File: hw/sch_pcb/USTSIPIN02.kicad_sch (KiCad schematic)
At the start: 5 parts, among them M1 HOLE, M2 HOLE, M3 HOLE, M4 HOLE, M8 BMI-S-204-F

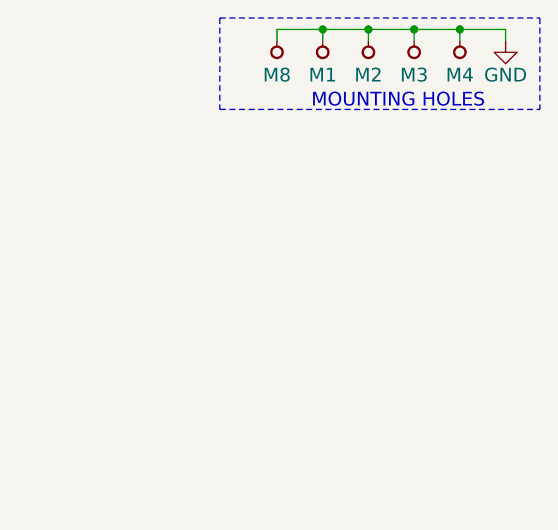
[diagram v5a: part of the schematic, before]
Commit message: Angled USB IC.
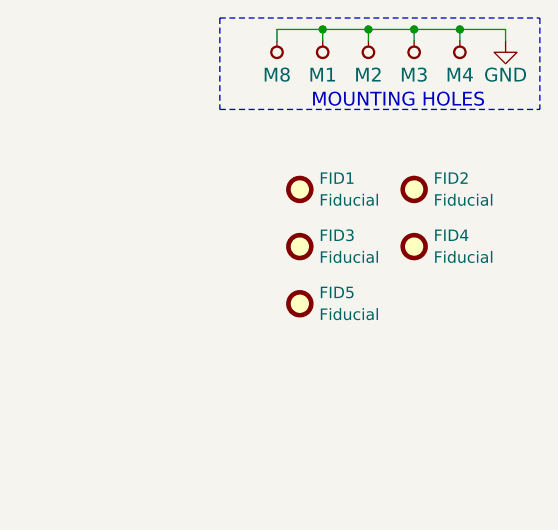
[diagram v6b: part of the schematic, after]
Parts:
- added FID1, FID2, FID3, FID4, FID5: Fiducial, Fiducial:Fiducial_1mm_Mask2mm, symbol Mechanical:Fiducial
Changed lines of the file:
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@@
+    )
+  )
+  (symbol (lib_id "Mechanical:Fiducial") (at 255.27 40.64 0) (unit 1)
+    (in_bom yes) (on_board yes) (dnp no) (fields_autoplaced)
+    (property "Reference" "FID3" (at 257.429 39.4279 0)
+      (effects (font (size 1.27 1.27)) (justify left))
+    )
+    (property "Value" "Fiducial" (at 257.429 41.8521 0)
+      (effects (font (size 1.27 1.27)) (justify left))
+    )
+    (property "Footprint" "Fiducial:Fiducial_1mm_Mask2mm" (at 255.27 40.64 0)
+      (effects (font (size 1.27 1.27)) hide)
+    )
+    (property "Datasheet" "~" (at 255.27 40.64 0)
+      (effects (font (size 1.27 1.27)) hide)
+    )
+    (instances
+      (project "USTSIPIN02"
+        (path "/0a87ced0-2af2-43c5-a56c-218f7013d76f"
+          (reference "FID3") (unit 1)
+        )
+      )
+      (project "PIND02"
+        (path "/2ae32537-a16f-4c5b-a56b-c6dddfb8ddb4"
+          (reference "FID1") (unit 1)
+        )
+      )
+      (project "AIRDOS04_base"
+        (path "/e63e39d7-6ac0-4ffd-8aa3-1841a4541b55/e191f86f-5b54-4b8b-aca6-37b81226f3b6"
+          (reference "FID3") (unit 1)
+        )
+        (path "/e63e39d7-6ac0-4ffd-8aa3-1841a4541b55"
+          (reference "FID3") (unit 1)
+        )
+      )
+    )
+  )
+  (symbol (lib_id "Mechanical:Fiducial") (at 255.27 34.29 0) (unit 1)
+    (in_bom yes) (on_board yes) (dnp no) (fields_autoplaced)
+    (property "Reference" "FID1" (at 257.429 33.0779 0)
+      (effects (font (size 1.27 1.27)) (justify left))
+    )
+    (property "Value" "Fiducial" (at 257.429 35.5021 0)
+      (effects (font (size 1.27 1.27)) (justify left))
+    )
+    (property "Footprint" "Fiducial:Fiducial_1mm_Mask2mm" (at 255.27 34.29 0)
+      (effects (font (size 1.27 1.27)) hide)
+    )
+    (property "Datasheet" "~" (at 255.27 34.29 0)
+      (effects (font (size 1.27 1.27)) hide)
+    )
+    (instances
+      (project "USTSIPIN02"
+        (path "/0a87ced0-2af2-43c5-a56c-218f7013d76f"
+          (reference "FID1") (unit 1)
+        )
+      )
+      (project "AIRDOS04_base"
+        (path "/e63e39d7-6ac0-4ffd-8aa3-1841a4541b55"
+          (reference "FID1") (unit 1)
+        )
+        (path "/e63e39d7-6ac0-4ffd-8aa3-1841a4541b55/5c006114-f78d-4936-a365-c4e7307459e1"
+          (reference "FID1") (unit 1)
+        )
+      )
+    )
+  )
+  (symbol (lib_id "Mechanical:Fiducial") (at 267.97 34.29 0) (unit 1)
+    (in_bom yes) (on_board yes) (dnp no) (fields_autoplaced)
+    (property "Reference" "FID2" (at 270.129 33.0779 0)
+      (effects (font (size 1.27 1.27)) (justify left))
+    )
+    (property "Value" "Fiducial" (at 270.129 35.5021 0)
+      (effects (font (size 1.27 1.27)) (justify left))
+    )
+    (property "Footprint" "Fiducial:Fiducial_1mm_Mask2mm" (at 267.97 34.29 0)
+      (effects (font (size 1.27 1.27)) hide)
+    )
+    (property "Datasheet" "~" (at 267.97 34.29 0)
+      (effects (font (size 1.27 1.27)) hide)
+    )
+    (instances
+      (project "USTSIPIN02"
+        (path "/0a87ced0-2af2-43c5-a56c-218f7013d76f"
+          (reference "FID2") (unit 1)
+        )
+      )
+      (project "AIRDOS04_base"
+        (path "/e63e39d7-6ac0-4ffd-8aa3-1841a4541b55"
+          (reference "FID2") (unit 1)
+        )
+        (path "/e63e39d7-6ac0-4ffd-8aa3-1841a4541b55/5c006114-f78d-4936-a365-c4e7307459e1"
+          (reference "FID2") (unit 1)
+        )
+      )
+    )
+  )
+  (symbol (lib_id "Mechanical:Fiducial") (at 267.97 40.64 0) (unit 1)
+    (in_bom yes) (on_board yes) (dnp no) (fields_autoplaced)
+    (property "Reference" "FID4" (at 270.129 39.4279 0)
+      (effects (font (size 1.27 1.27)) (justify left))
+    )
+    (property "Value" "Fiducial" (at 270.129 41.8521 0)
+      (effects (font (size 1.27 1.27)) (justify left))
+    )
+    (property "Footprint" "Fiducial:Fiducial_1mm_Mask2mm" (at 267.97 40.64 0)
+      (effects (font (size 1.27 1.27)) hide)
+    )
+    (property "Datasheet" "~" (at 267.97 40.64 0)
+      (effects (font (size 1.27 1.27)) hide)
+    )
+    (instances
+      (project "USTSIPIN02"
+        (path "/0a87ced0-2af2-43c5-a56c-218f7013d76f"
+          (reference "FID4") (unit 1)
+        )
+      )
+      (project "PIND02"
+        (path "/2ae32537-a16f-4c5b-a56b-c6dddfb8ddb4"
+          (reference "FID2") (unit 1)
+        )
+      )
+      (project "AIRDOS04_base"
+        (path "/e63e39d7-6ac0-4ffd-8aa3-1841a4541b55/e191f86f-5b54-4b8b-aca6-37b81226f3b6"
+          (reference "FID4") (unit 1)
+        )
+        (path "/e63e39d7-6ac0-4ffd-8aa3-1841a4541b55"
+          (reference "FID4") (unit 1)
+        )
+      )
+    )
+  )
+  (symbol (lib_id "Mechanical:Fiducial") (at 255.27 46.99 0) (unit 1)
+    (in_bom yes) (on_board yes) (dnp no) (fields_autoplaced)
+    (property "Reference" "FID5" (at 257.429 45.7779 0)
+      (effects (font (size 1.27 1.27)) (justify left))
+    )
+    (property "Value" "Fiducial" (at 257.429 48.2021 0)
+      (effects (font (size 1.27 1.27)) (justify left))
+    )
+    (property "Footprint" "Fiducial:Fiducial_1mm_Mask2mm" (at 255.27 46.99 0)
+      (effects (font (size 1.27 1.27)) hide)
+    )
+    (property "Datasheet" "~" (at 255.27 46.99 0)
+      (effects (font (size 1.27 1.27)) hide)
+    )
+    (instances
+      (project "USTSIPIN02"
+        (path "/0a87ced0-2af2-43c5-a56c-218f7013d76f"
+          (reference "FID5") (unit 1)
+        )
+      )
+      (project "PIND02"
+        (path "/2ae32537-a16f-4c5b-a56b-c6dddfb8ddb4"
+          (reference "FID2") (unit 1)
+        )
+      )
+      (project "AIRDOS04_base"
+        (path "/e63e39d7-6ac0-4ffd-8aa3-1841a4541b55/e191f86f-5b54-4b8b-aca6-37b81226f3b6"
+          (reference "FID4") (unit 1)
+        )
+        (path "/e63e39d7-6ac0-4ffd-8aa3-1841a4541b55"
+          (reference "FID4") (unit 1)
+        )
+      )
     )
   )

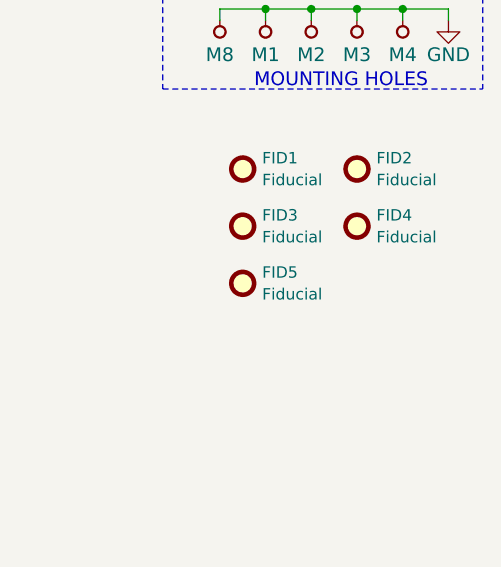
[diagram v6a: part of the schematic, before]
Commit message: Improve clearance issues on USB chip power supply.
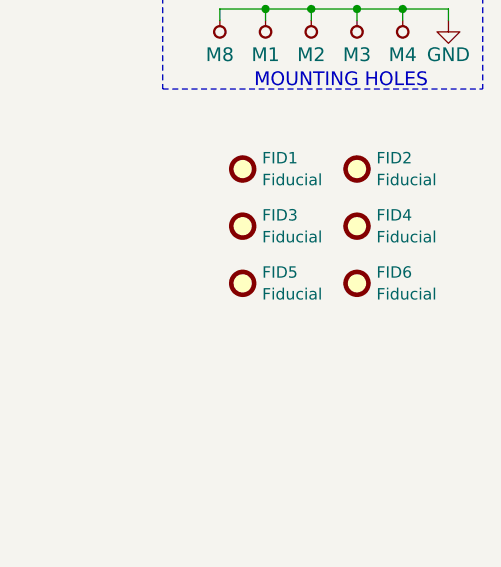
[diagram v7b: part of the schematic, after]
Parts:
- added FID6: Fiducial, Fiducial:Fiducial_1mm_Mask2mm, symbol Mechanical:Fiducial
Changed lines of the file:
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@@
+    )
+  )
+  (symbol (lib_id "Mechanical:Fiducial") (at 267.97 46.99 0) (unit 1)
+    (in_bom yes) (on_board yes) (dnp no) (fields_autoplaced)
+    (property "Reference" "FID6" (at 270.129 45.7779 0)
+      (effects (font (size 1.27 1.27)) (justify left))
+    )
+    (property "Value" "Fiducial" (at 270.129 48.2021 0)
+      (effects (font (size 1.27 1.27)) (justify left))
+    )
+    (property "Footprint" "Fiducial:Fiducial_1mm_Mask2mm" (at 267.97 46.99 0)
+      (effects (font (size 1.27 1.27)) hide)
+    )
+    (property "Datasheet" "~" (at 267.97 46.99 0)
+      (effects (font (size 1.27 1.27)) hide)
+    )
+    (instances
+      (project "USTSIPIN02"
+        (path "/0a87ced0-2af2-43c5-a56c-218f7013d76f"
+          (reference "FID6") (unit 1)
+        )
+      )
+      (project "PIND02"
+        (path "/2ae32537-a16f-4c5b-a56b-c6dddfb8ddb4"
+          (reference "FID2") (unit 1)
+        )
+      )
+      (project "AIRDOS04_base"
+        (path "/e63e39d7-6ac0-4ffd-8aa3-1841a4541b55/e191f86f-5b54-4b8b-aca6-37b81226f3b6"
+          (reference "FID4") (unit 1)
+        )
+        (path "/e63e39d7-6ac0-4ffd-8aa3-1841a4541b55"
+          (reference "FID4") (unit 1)
+        )
+      )
     )
   )

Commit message: Resolve inconsistent component types.
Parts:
- FID1, FID2, FID3, FID4, FID5, FID6, M1, M2, M3, M4: now left out of the parts list
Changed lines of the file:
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@@
   )
   (symbol (lib_id "MLAB_MECHANICAL:HOLE") (at 262.89 19.05 90) (unit 1)
-    (in_bom yes) (on_board yes) (dnp no)
+    (in_bom no) (on_board yes) (dnp no)
     (property "Reference" "M2" (at 262.89 21.59 90)
       (effects (font (size 1.524 1.524)))
@@
       (effects (font (size 1.524 1.524)))
     )
+    (property "UST_ID" "" (at 262.89 19.05 0)
+      (effects (font (size 1.27 1.27)) hide)
+    )
     (pin "1")
     (instances
@@
   )
   (symbol (lib_id "MLAB_MECHANICAL:HOLE") (at 267.97 19.05 90) (unit 1)
-    (in_bom yes) (on_board yes) (dnp no)
+    (in_bom no) (on_board yes) (dnp no)
     (property "Reference" "M3" (at 267.97 21.59 90)
       (effects (font (size 1.524 1.524)))
@@
       (effects (font (size 1.524 1.524)))
     )
+    (property "UST_ID" "" (at 267.97 19.05 0)
+      (effects (font (size 1.27 1.27)) hide)
+    )
     (pin "1")
     (instances
@@
   )
   (symbol (lib_id "MLAB_MECHANICAL:HOLE") (at 273.05 19.05 90) (unit 1)
-    (in_bom yes) (on_board yes) (dnp no)
+    (in_bom no) (on_board yes) (dnp no)
     (property "Reference" "M4" (at 273.05 21.59 90)
       (effects (font (size 1.524 1.524)))
@@
     (property "Datasheet" "" (at 273.05 19.05 0)
       (effects (font (size 1.524 1.524)))
+    )
+    (property "UST_ID" "" (at 273.05 19.05 0)
+      (effects (font (size 1.27 1.27)) hide)
     )
     (pin "1")
@@
   )
   (symbol (lib_id "MLAB_MECHANICAL:HOLE") (at 257.81 19.05 90) (unit 1)
-    (in_bom yes) (on_board yes) (dnp no)
+    (in_bom no) (on_board yes) (dnp no)
     (property "Reference" "M1" (at 257.81 21.59 90)
       (effects (font (size 1.524 1.524)))
@@
     (property "Datasheet" "" (at 257.81 19.05 0)
       (effects (font (size 1.524 1.524)))
+    )
+    (property "UST_ID" "" (at 257.81 19.05 0)
+      (effects (font (size 1.27 1.27)) hide)
     )
     (pin "1")
@@
   )
   (symbol (lib_id "Mechanical:Fiducial") (at 255.27 40.64 0) (unit 1)
-    (in_bom yes) (on_board yes) (dnp no) (fields_autoplaced)
+    (in_bom no) (on_board yes) (dnp no) (fields_autoplaced)
     (property "Reference" "FID3" (at 257.429 39.4279 0)
       (effects (font (size 1.27 1.27)) (justify left))
@@
     )
     (property "Datasheet" "~" (at 255.27 40.64 0)
+      (effects (font (size 1.27 1.27)) hide)
+    )
+    (property "UST_ID" "" (at 255.27 40.64 0)
       (effects (font (size 1.27 1.27)) hide)
     )
@@
   )
   (symbol (lib_id "Mechanical:Fiducial") (at 255.27 34.29 0) (unit 1)
-    (in_bom yes) (on_board yes) (dnp no) (fields_autoplaced)
+    (in_bom no) (on_board yes) (dnp no) (fields_autoplaced)
     (property "Reference" "FID1" (at 257.429 33.0779 0)
       (effects (font (size 1.27 1.27)) (justify left))
@@
     )
     (property "Datasheet" "~" (at 255.27 34.29 0)
+      (effects (font (size 1.27 1.27)) hide)
+    )
+    (property "UST_ID" "" (at 255.27 34.29 0)
       (effects (font (size 1.27 1.27)) hide)
     )
@@
   )
   (symbol (lib_id "Mechanical:Fiducial") (at 267.97 34.29 0) (unit 1)
-    (in_bom yes) (on_board yes) (dnp no) (fields_autoplaced)
+    (in_bom no) (on_board yes) (dnp no) (fields_autoplaced)
     (property "Reference" "FID2" (at 270.129 33.0779 0)
       (effects (font (size 1.27 1.27)) (justify left))
@@
       (effects (font (size 1.27 1.27)) hide)
     )
+    (property "UST_ID" "" (at 267.97 34.29 0)
+      (effects (font (size 1.27 1.27)) hide)
+    )
     (instances
       (project "USTSIPIN02"
@@
   )
   (symbol (lib_id "Mechanical:Fiducial") (at 267.97 46.99 0) (unit 1)
-    (in_bom yes) (on_board yes) (dnp no) (fields_autoplaced)
+    (in_bom no) (on_board yes) (dnp no) (fields_autoplaced)
     (property "Reference" "FID6" (at 270.129 45.7779 0)
       (effects (font (size 1.27 1.27)) (justify left))
@@
     )
     (property "Datasheet" "~" (at 267.97 46.99 0)
+      (effects (font (size 1.27 1.27)) hide)
+    )
+    (property "UST_ID" "" (at 267.97 46.99 0)
       (effects (font (size 1.27 1.27)) hide)
     )
@@
   )
   (symbol (lib_id "Mechanical:Fiducial") (at 267.97 40.64 0) (unit 1)
-    (in_bom yes) (on_board yes) (dnp no) (fields_autoplaced)
+    (in_bom no) (on_board yes) (dnp no) (fields_autoplaced)
     (property "Reference" "FID4" (at 270.129 39.4279 0)
       (effects (font (size 1.27 1.27)) (justify left))
@@
     )
     (property "Datasheet" "~" (at 267.97 40.64 0)
+      (effects (font (size 1.27 1.27)) hide)
+    )
+    (property "UST_ID" "" (at 267.97 40.64 0)
       (effects (font (size 1.27 1.27)) hide)
     )
@@
   )
   (symbol (lib_id "Mechanical:Fiducial") (at 255.27 46.99 0) (unit 1)
-    (in_bom yes) (on_board yes) (dnp no) (fields_autoplaced)
+    (in_bom no) (on_board yes) (dnp no) (fields_autoplaced)
     (property "Reference" "FID5" (at 257.429 45.7779 0)
       (effects (font (size 1.27 1.27)) (justify left))
@@
       (effects (font (size 1.27 1.27)) hide)
     )
+    (property "UST_ID" "" (at 255.27 46.99 0)
+      (effects (font (size 1.27 1.27)) hide)
+    )
